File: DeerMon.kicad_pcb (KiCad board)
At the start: 4 copper layers, 30 x 45 mm, 62 parts, among them J1 TYPE-C-31-M-12, J2 ZJY144S025, J3 GPIO, M1 Mark, M2 Mark, M3 Mark, M4 Mark, P1 Position, P2 Position, P3 Position, P4 Position, P5 Position, Q1 DDC114TH, Q2 2N7002, SW1 BOOT, SW2 EN, U1 CP2102N-A02-GQFN24R, U2 AW9364DNR, U3 SPX3819M5-L-3-3, U4 ESP32-PICO-V3-02

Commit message: Update for RGB
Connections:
- net /RMT_RGB renamed /RGB
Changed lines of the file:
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@@
   (net 37 /IO5)
   (net 38 "Net-(R10-Pad2)")
-  (net 39 /RMT_RGB)
+  (net 39 /RGB)
   (net_class Default "This is the default net class."
     (clearance 0.15)
@@
     (add_net /LCD_SDA)
     (add_net /LEDK)
-    (add_net /RMT_RGB)
+    (add_net /RGB)
     (add_net /RTS)
     (add_net /USB_RX)
@@
     )
     (pad 2 smd roundrect (at 0.51 0) (size 0.54 0.64) (layers F.Cu F.Paste F.Mask) (roundrect_rratio 0.25)
-      (net 39 /RMT_RGB))
+      (net 39 /RGB))
     (pad 1 smd roundrect (at -0.51 0) (size 0.54 0.64) (layers F.Cu F.Paste F.Mask) (roundrect_rratio 0.25)
       (net 3 +3V3))
@@
       (net 2 GND))
     (pad 3 smd rect (at 0.45 0.45 90) (size 0.5 0.5) (layers F.Cu F.Paste F.Mask)
-      (net 39 /RMT_RGB))
+      (net 39 /RGB))
     (pad 4 smd rect (at 0.45 -0.45 90) (size 0.5 0.5) (layers F.Cu F.Paste F.Mask)
       (net 3 +3V3))
@@
       (net 3 +3V3))
     (pad 42 smd roundrect (at 0.25 -3.4375 135) (size 0.25 0.875) (layers F.Cu F.Paste F.Mask) (roundrect_rratio 0.25)
-      (net 39 /RMT_RGB))
+      (net 39 /RGB))
     (pad 41 smd roundrect (at 0.75 -3.4375 135) (size 0.25 0.875) (layers F.Cu F.Paste F.Mask) (roundrect_rratio 0.25)
       (net 22 /ESP_TX))

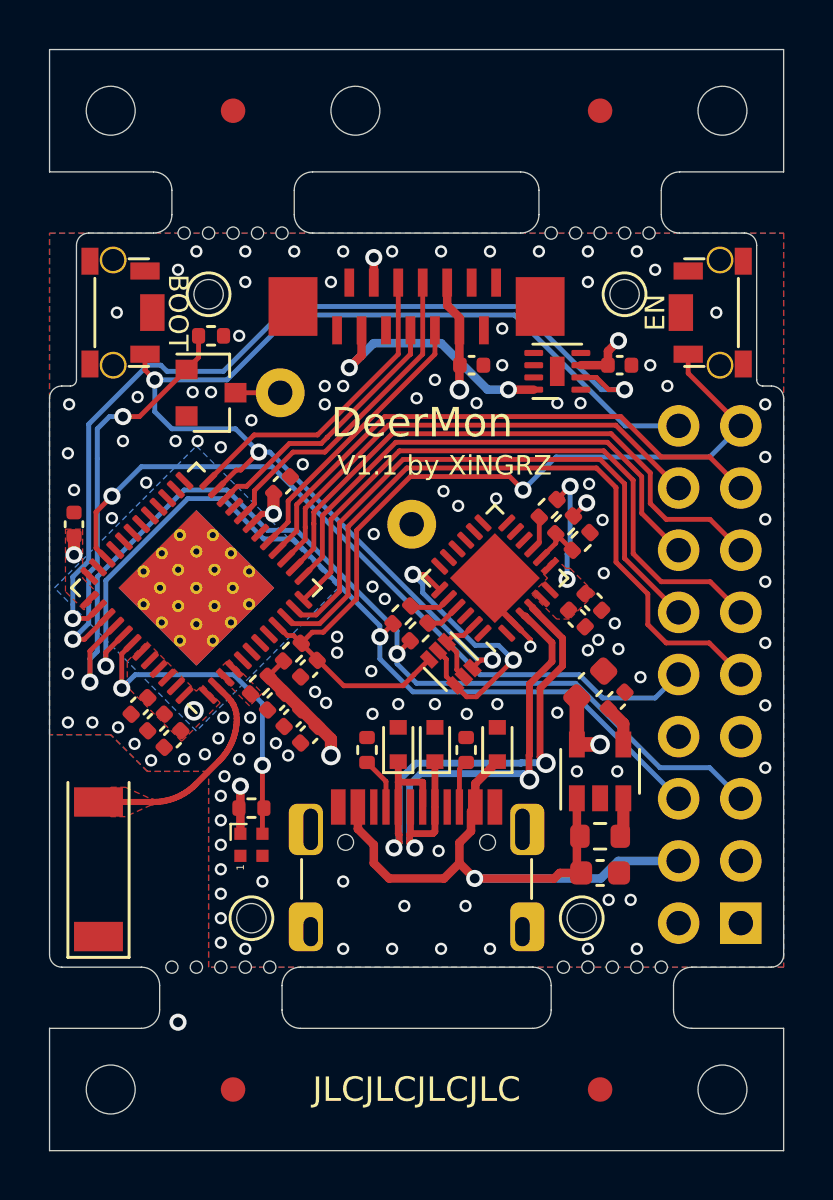
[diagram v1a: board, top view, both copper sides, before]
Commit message: Drop position holes, let JLC add it
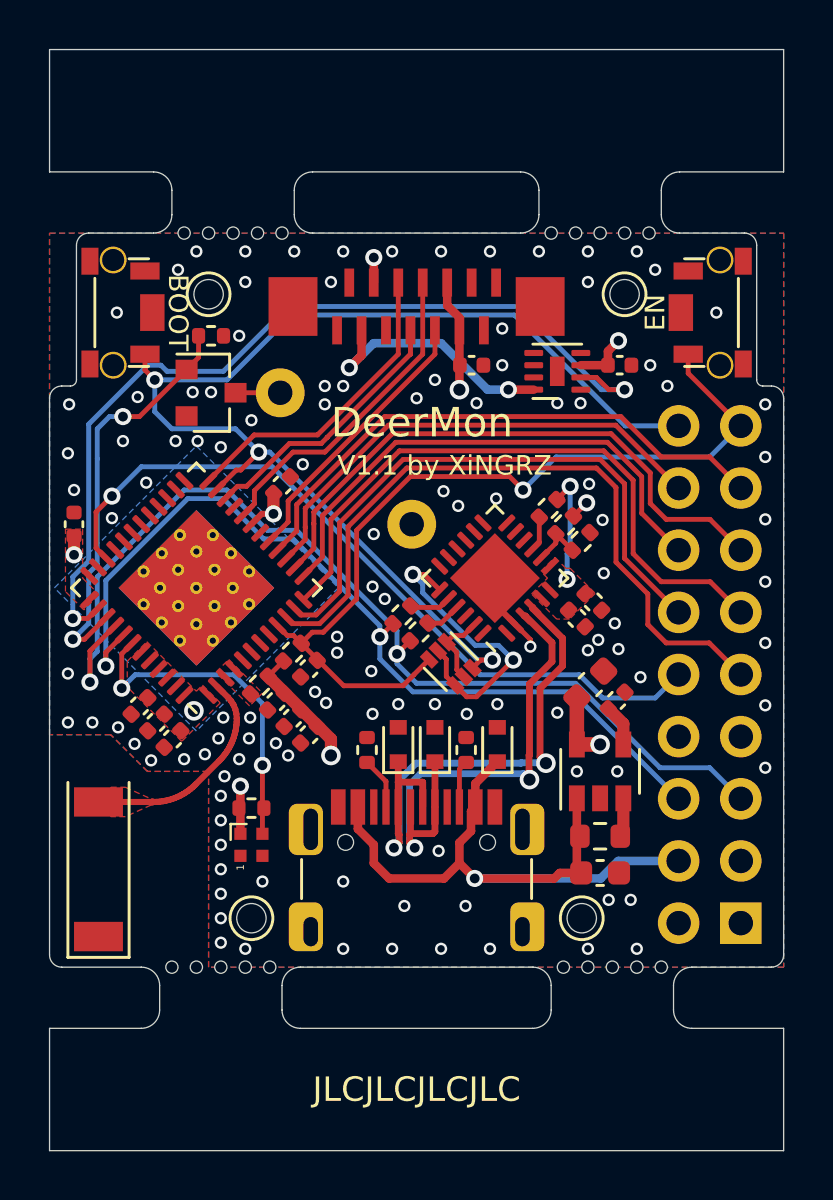
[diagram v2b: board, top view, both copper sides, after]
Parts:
- removed M1, M2, M3, M4: Mark, JLC-SMT:JLC_MARK
- removed P1, P2, P3, P4, P5: Position, JLC-SMT:JLC_POS
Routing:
- net (no net): vias 1 -> 0
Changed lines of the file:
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@@
     (thickness 1.6)
     (drawings 100)
-    (tracks 581)
+    (tracks 580)
     (zones 0)
-    (modules 62)
+    (modules 53)
     (nets 40)
   )
@@
     (pad "" np_thru_hole circle (at 0 0) (size 1.2 1.2) (drill 1.2) (layers *.Cu *.Mask))
   )
-  (module JLC-SMT:JLC_POS (layer F.Cu)
-    (at 62.5 45)
-    (attr virtual)
-    (fp_text reference P5 (at 0 2) (layer F.Fab)
-      (effects (font (size 1 1) (thickness 0.15)))
-    )
-    (fp_text value Position (at 0 -2) (layer F.Fab)
-      (effects (font (size 1 1) (thickness 0.15)))
-    )
-    (pad "" np_thru_hole circle (at 0 0) (size 2 2) (drill 2) (layers *.Cu *.Mask))
-  )
-  (module JLC-SMT:JLC_POS (layer F.Cu)
-    (at 52.5 45)
-    (attr virtual)
-    (fp_text reference P4 (at 0 2) (layer F.Fab)
-      (effects (font (size 1 1) (thickness 0.15)))
-    )
-    (fp_text value Position (at 0 -2) (layer F.Fab)
-      (effects (font (size 1 1) (thickness 0.15)))
-    )
-    (pad "" np_thru_hole circle (at 0 0) (size 2 2) (drill 2) (layers *.Cu *.Mask))
-  )
-  (module JLC-SMT:JLC_POS (layer F.Cu)
-    (at 77.5 45)
-    (attr virtual)
-    (fp_text reference P3 (at 0 2) (layer F.Fab)
-      (effects (font (size 1 1) (thickness 0.15)))
-    )
-    (fp_text value Position (at 0 -2) (layer F.Fab)
-      (effects (font (size 1 1) (thickness 0.15)))
-    )
-    (pad "" np_thru_hole circle (at 0 0) (size 2 2) (drill 2) (layers *.Cu *.Mask))
-  )
-  (module JLC-SMT:JLC_POS (layer F.Cu)
-    (at 52.5 85)
-    (attr virtual)
-    (fp_text reference P2 (at 0 2) (layer F.Fab)
-      (effects (font (size 1 1) (thickness 0.15)))
-    )
-    (fp_text value Position (at 0 -2) (layer F.Fab)
-      (effects (font (size 1 1) (thickness 0.15)))
-    )
-    (pad "" np_thru_hole circle (at 0 0) (size 2 2) (drill 2) (layers *.Cu *.Mask))
-  )
-  (module JLC-SMT:JLC_POS (layer F.Cu)
-    (at 77.5 85)
-    (attr virtual)
-    (fp_text reference P1 (at 0 2) (layer F.Fab)
-      (effects (font (size 1 1) (thickness 0.15)))
-    )
-    (fp_text value Position (at 0 -2) (layer F.Fab)
-      (effects (font (size 1 1) (thickness 0.15)))
-    )
-    (pad "" np_thru_hole circle (at 0 0) (size 2 2) (drill 2) (layers *.Cu *.Mask))
-  )
-  (module JLC-SMT:JLC_MARK (layer F.Cu)
-    (at 72.5 85)
-    (attr virtual)
-    (fp_text reference M4 (at 0 2) (layer F.Fab)
-      (effects (font (size 1 1) (thickness 0.15)))
-    )
-    (fp_text value Mark (at 0 -2) (layer F.Fab)
-      (effects (font (size 1 1) (thickness 0.15)))
-    )
-    (pad 1 smd circle (at 0 0) (size 1 1) (layers *.Paste *.Mask F.Cu)
-      (solder_mask_margin 0.5))
-  )
-  (module JLC-SMT:JLC_MARK (layer F.Cu)
-    (at 72.5 45)
-    (attr virtual)
-    (fp_text reference M3 (at 0 2) (layer F.Fab)
-      (effects (font (size 1 1) (thickness 0.15)))
-    )
-    (fp_text value Mark (at 0 -2) (layer F.Fab)
-      (effects (font (size 1 1) (thickness 0.15)))
-    )
-    (pad 1 smd circle (at 0 0) (size 1 1) (layers *.Paste *.Mask F.Cu)
-      (solder_mask_margin 0.5))
-  )
-  (module JLC-SMT:JLC_MARK (layer F.Cu)
-    (at 57.5 85)
-    (attr virtual)
-    (fp_text reference M2 (at 0 2) (layer F.Fab)
-      (effects (font (size 1 1) (thickness 0.15)))
-    )
-    (fp_text value Mark (at 0 -2) (layer F.Fab)
-      (effects (font (size 1 1) (thickness 0.15)))
-    )
-    (pad 1 smd circle (at 0 0) (size 1 1) (layers *.Paste *.Mask F.Cu)
-      (solder_mask_margin 0.5))
-  )
-  (module JLC-SMT:JLC_MARK (layer F.Cu)
-    (at 57.5 45)
-    (attr virtual)
-    (fp_text reference M1 (at 0 2) (layer F.Fab)
-      (effects (font (size 1 1) (thickness 0.15)))
-    )
-    (fp_text value Mark (at 0 -2) (layer F.Fab)
-      (effects (font (size 1 1) (thickness 0.15)))
-    )
-    (pad 1 smd circle (at 0 0) (size 1 1) (layers *.Paste *.Mask F.Cu)
-      (solder_mask_margin 0.5))
-  )
   (module JLC-SMT:HNDZ_TMB1206-05 locked (layer B.Cu)
     (at 64.8 61.9 135)
@@
     (arrow2b (pts (xy 50 37.5) (xy 51.126504 36.913579)))
   )
-  (via (at 55.25 82.25) (size 0.7) (drill 0.4) (layers F.Cu B.Cu) (net 0))
   (segment (start 57.635137 69.643147) (end 57.65 69.831981) (width 0.25) (layer F.Cu) (net 1))
   (segment (start 57.590919 69.458964) (end 57.635137 69.643147) (width 0.25) (layer F.Cu) (net 1))

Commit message: Better vias
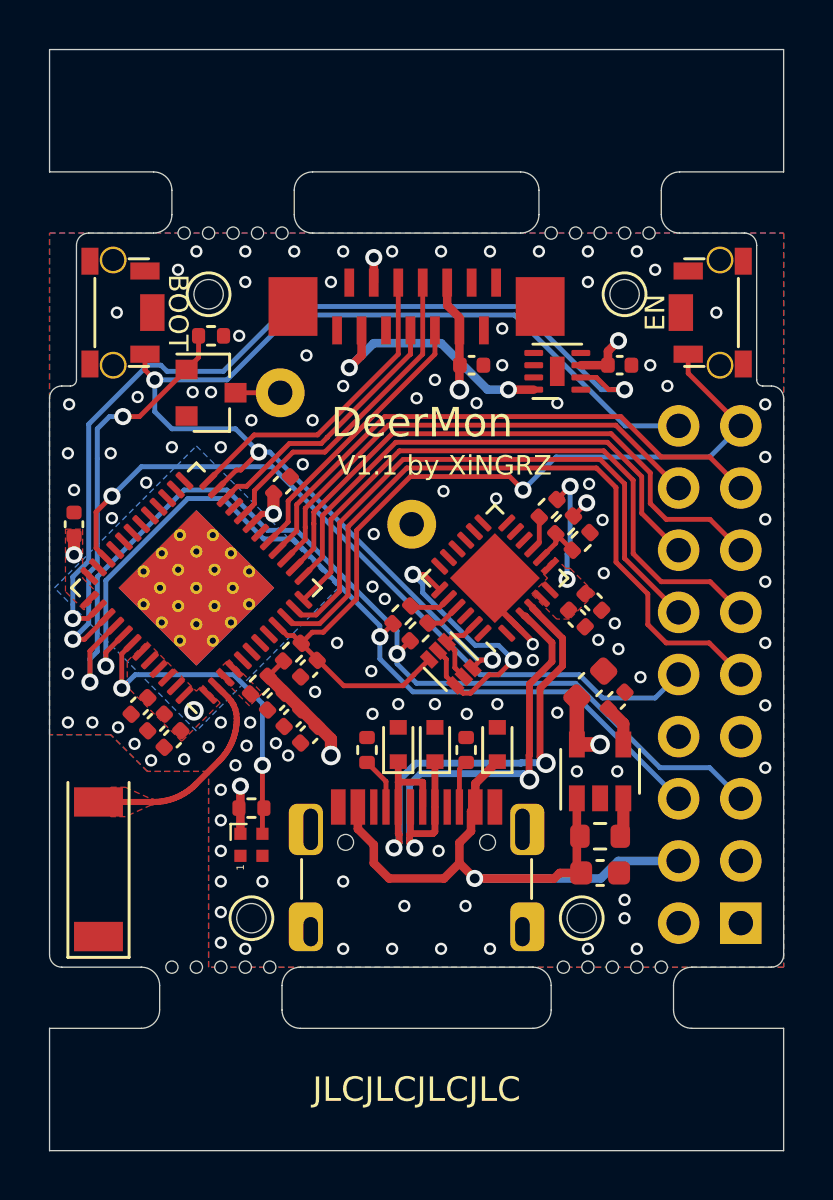
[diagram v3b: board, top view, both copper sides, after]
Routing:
- net GND: track 3.40 -> 3.34 mm, vias 116 -> 108

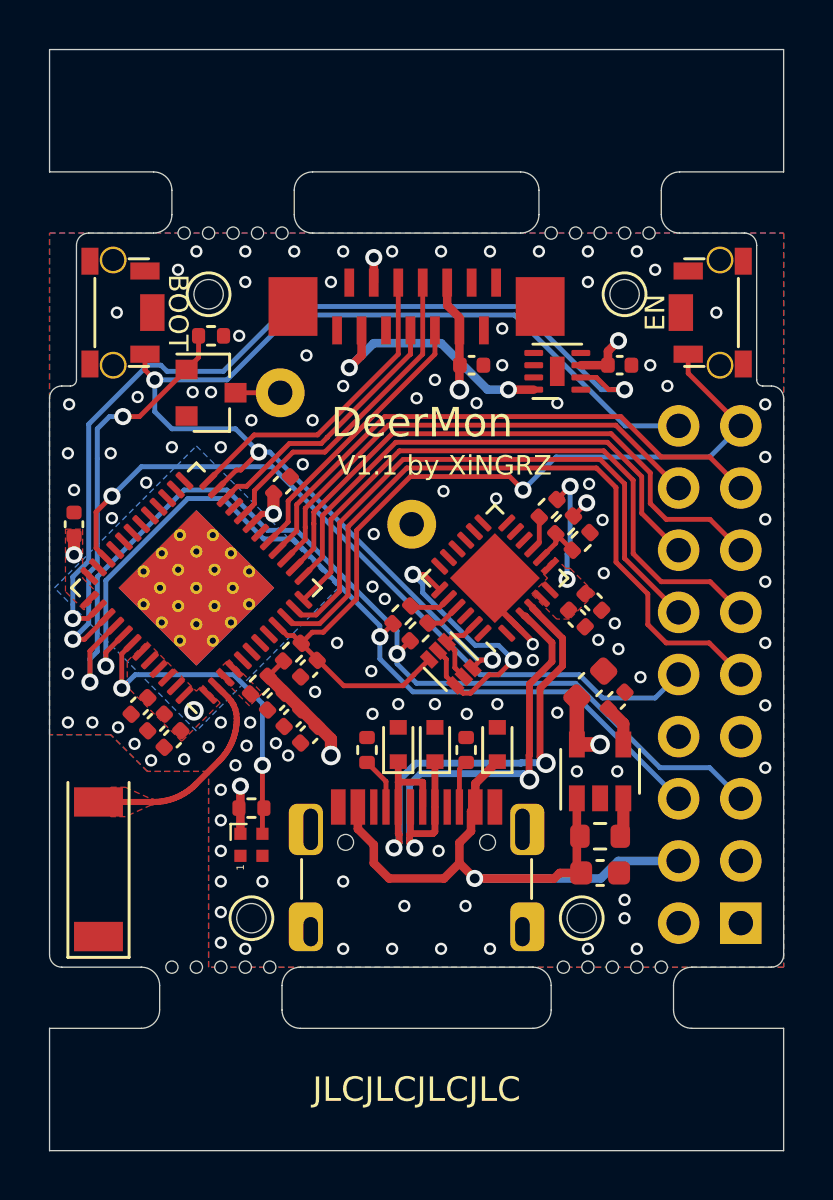
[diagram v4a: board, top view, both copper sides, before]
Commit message: Replace DDC114TH with PUMH4
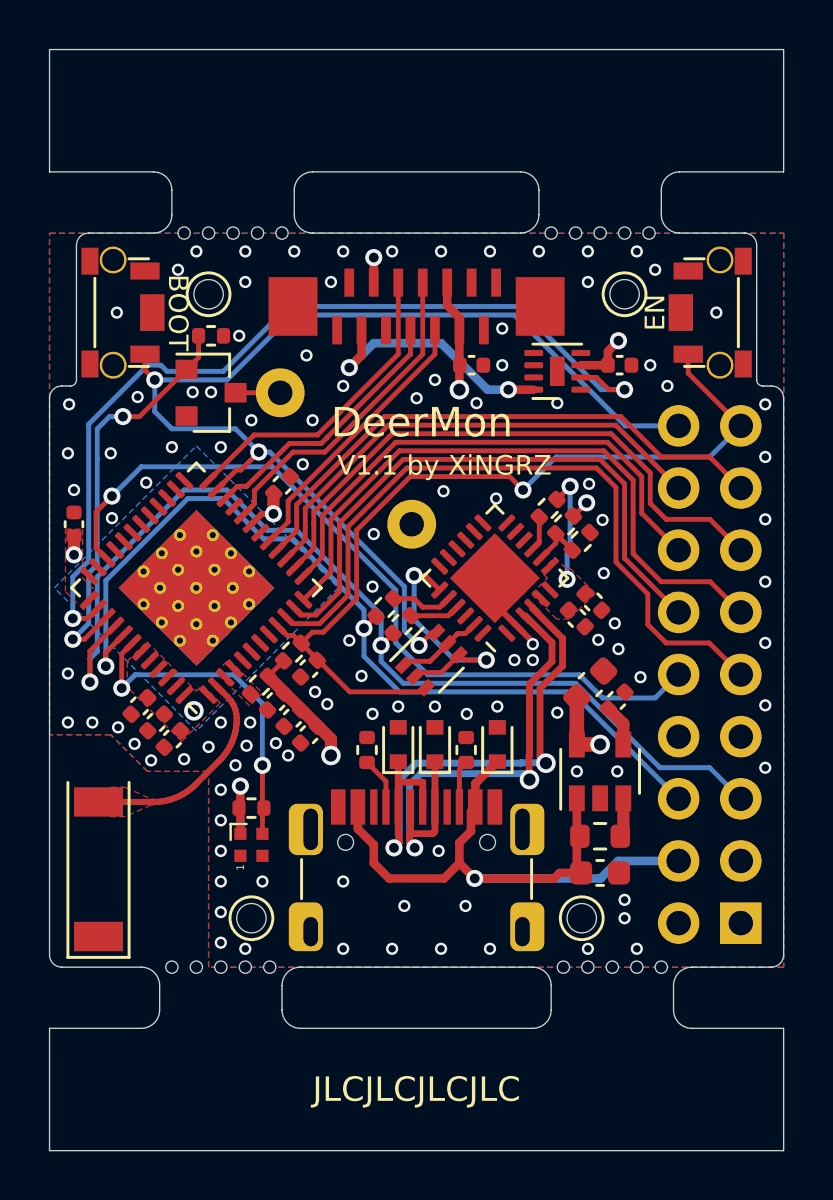
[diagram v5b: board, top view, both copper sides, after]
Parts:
- Q1: value DDC114TH -> PUMH4; footprint Package_TO_SOT_SMD:SOT-563 -> Package_TO_SOT_SMD:SOT-363_SC-70-6
- moved Q1 0.81 mm to (65.6, 67.5), turned to 45 degrees
- moved R7 0.76 mm to (63.7, 65.3)
- moved R8 0.76 mm to (64.4, 66.0)
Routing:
- net /BOOT: track 48.2 -> 46.0 mm
- net /RTS: track 11.9 -> 10.1 mm
- net /IO5: track 31.5 -> 32.7 mm
- net /USB_RX: track 1.63 -> 2.53 mm
- net +3V3: track 114.3 -> 115.1 mm
- net /USB_TX: track 1.46 -> 2.04 mm
- net GND: vias 108 -> 109

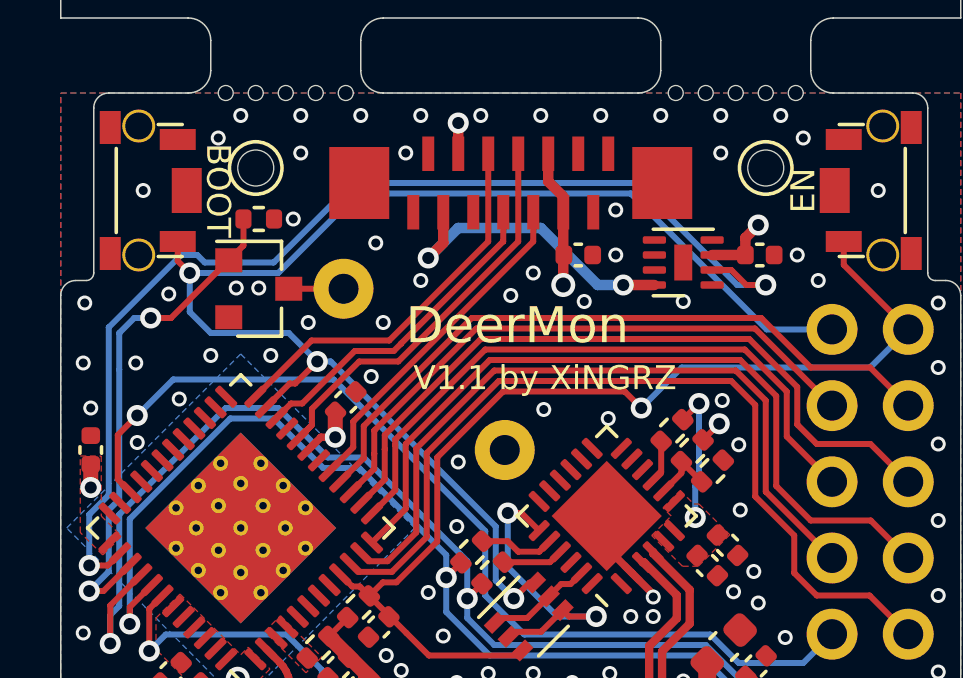
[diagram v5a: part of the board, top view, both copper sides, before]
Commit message: Replace AW9364 with BCT3220
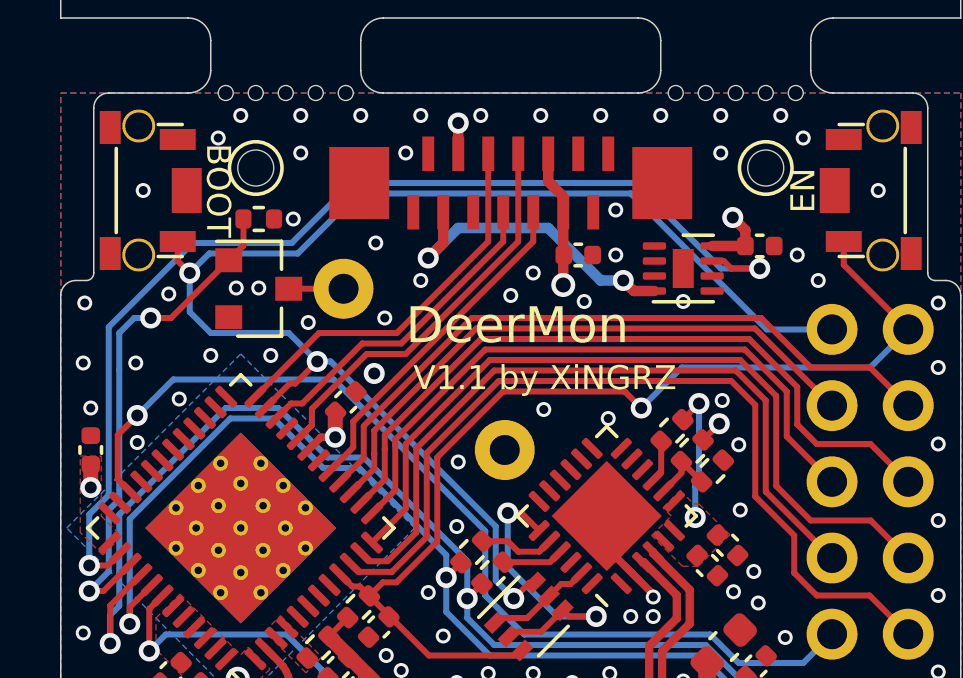
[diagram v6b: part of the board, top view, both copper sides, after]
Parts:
- U2: value AW9364DNR -> BCT3220ELA-TR; footprint JLC-SMT:AW9364DNR_DFN2x2-8L -> Package_DFN_QFN:DFN-8-1EP_2x2mm_P0.5mm_EP0.7x1.3mm
- moved C8 0.30 mm to (73.3, 55.1)
- moved U2 0.20 mm to (70.8, 55.9), turned to 0 degrees
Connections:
- U2 pad 1: GND -> (no net)
- U2 pad 2: /BLK -> (no net)
- U2 pad 3: +3V3 -> (no net)
- U2 pad 4: GND -> /LEDK
- U2 pad 5: (no net) -> GND
- U2 pad 6: (no net) -> GND
- U2 pad 7: (no net) -> /BLK
- U2 pad 8: /LEDK -> +3V3
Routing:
- net /BLK: track 36.9 -> 36.0 mm
- net +3V3: track 115.1 -> 114.3 mm
